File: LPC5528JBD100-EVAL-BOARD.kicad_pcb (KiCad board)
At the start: 2 copper layers, 100 x 100 mm, 45 parts, among them J1 Jack-DC, J2 USB_B_Micro, J3 MCU_VOLTAGE_SEL, U1 LM2596S-5, U2 LPC55S28JBD100, U3 LM1117-3.3, U4 LM1117-1.8, U5 TPS2552DBVR, Y1 24MHz

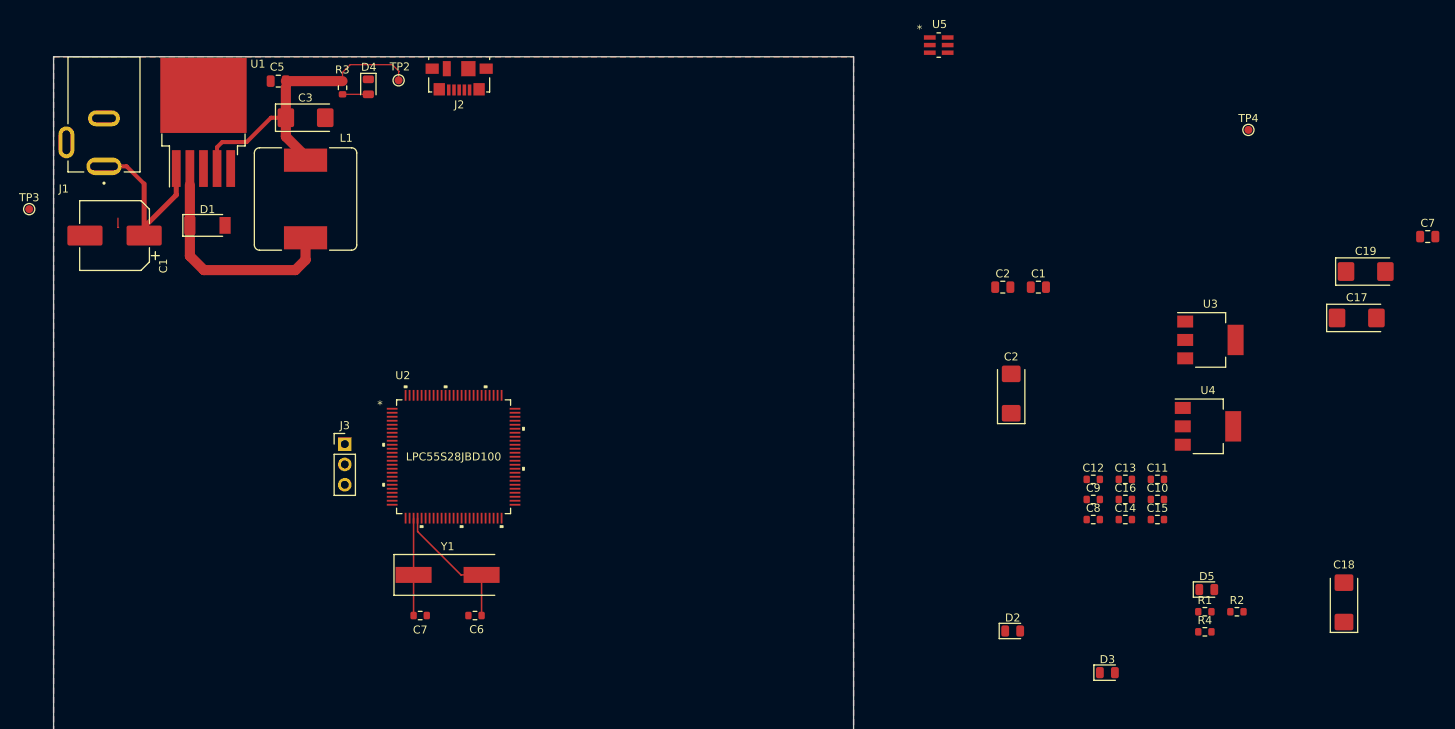
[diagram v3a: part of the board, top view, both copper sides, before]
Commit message: USB Current limiting devresi tamamlanacak. ADC bağlantıları yapılıyor
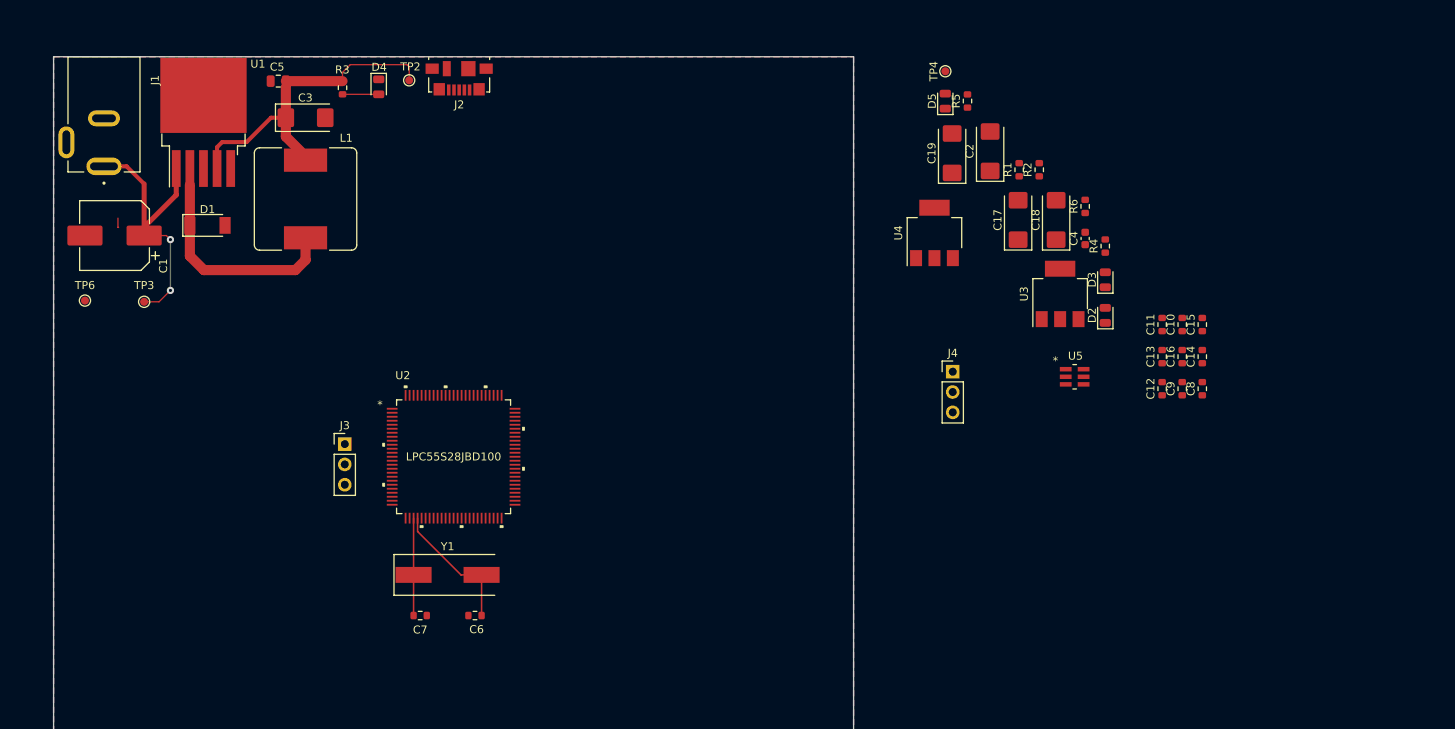
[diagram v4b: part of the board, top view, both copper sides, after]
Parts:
- removed the C1 at (123.1, 28.8)
- removed the C2 at (119.7, 42.1)
- removed the C2 at (118.7, 28.8)
- removed the C7 at (171.8, 22.5)
- added C2: 10uF, Capacitor_Tantalum_SMD:CP_EIA-6032-28_Kemet-C, F.Cu at (117.1, 11.8)
- added C4: 0.1uF, Capacitor_SMD:C_0603_1608Metric, F.Cu at (128.9, 22.7)
- added J4: ADC_V_SELECT, Connector_PinHeader_2.54mm:PinHeader_1x03_P2.54mm_Vertical, F.Cu at (112.4, 39.4)
- added R5: 20k, Resistor_SMD:R_0603_1608Metric, F.Cu at (114.2, 5.54)
- added R6: 100k, Resistor_SMD:R_0603_1608Metric, F.Cu at (128.9, 18.7)
- added TP6: TP_GND, TestPoint:TestPoint_Pad_D1.0mm, F.Cu at (3.92, 30.5)
- J3: value MCU_VOLTAGE_SEL -> MCU_V_SEL
- moved D5 69.3 mm to (111.5, 5.55), turned to 90 degrees
- moved R2 60.5 mm to (123.2, 14.1), turned to 90 degrees
- moved R1 59.9 mm to (120.7, 14.1), turned to 90 degrees
- moved C18 59.8 mm to (125.3, 20.4)
- moved C19 53.8 mm to (112.3, 12.1), turned to 90 degrees
- moved R4 49.8 mm to (131.5, 23.7), turned to 90 degrees
- moved D3 49.1 mm to (131.5, 27.9), turned to 90 degrees
- moved U5 44.8 mm to (127.6, 40.0)
- moved C17 44.1 mm to (120.6, 20.4), turned to 90 degrees
- moved U4 41.9 mm to (110.1, 22.0), turned to 90 degrees
- moved D2 41.1 mm to (131.5, 32.3), turned to 90 degrees
- moved TP4 38.6 mm to (111.5, 1.82), turned to 90 degrees
- moved C15 25.0 mm to (143.6, 33.5), turned to 90 degrees
- moved C14 22.5 mm to (143.6, 37.5), turned to 90 degrees
- moved C10 22.1 mm to (141.1, 33.5), turned to 90 degrees
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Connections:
- C10 pad 1: +3V3 -> V_TARGET
- C11 pad 1: +3V3 -> V_TARGET
- C12 pad 1: +3V3 -> V_TARGET
- C13 pad 1: +3V3 -> V_TARGET
- C14 pad 1: +3V3 -> V_TARGET
- C15 pad 1: +3V3 -> V_TARGET
- C16 pad 1: +3V3 -> V_TARGET
- C8 pad 1: +3V3 -> V_TARGET
- C9 pad 1: +3V3 -> V_TARGET
- U2 pad 17: unconnected-(U2-Pad17) -> /MCU/MCU_VREFP
- U2 pad 18: unconnected-(U2-Pad18) -> /MCU/MCU_VREFN
- U5 pad 4: unconnected-(U5-Pad4) -> /Power/USB_FAULT
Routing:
- net V_IN: track 22.4 -> 36.1 mm, vias 0 -> 2
- net +5V: track 37.8 -> 39.3 mm
- net Net-(D4-Pad2): track 3.23 -> 4.52 mm

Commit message: MCU bölümlere ayrýldý
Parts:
- added C21: 47pF, Resistor_SMD:R_0603_1608Metric, F.Cu at (175.6, 76.0)
- added C22: 0.1uF, Resistor_SMD:R_0603_1608Metric, F.Cu at (156.1, 94.8)
- added C6: 18pF, Resistor_SMD:R_0603_1608Metric, F.Cu at (195.1, 82.2)
- added C7: 18pF, Resistor_SMD:R_0603_1608Metric, F.Cu at (191.1, 82.2)
- added J3: ADC_EXT_SUPPLY, Connector_PinHeader_2.54mm:PinHeader_1x03_P2.54mm_Vertical, F.Cu at (171.3, 86.7)
- added R10: 0, Resistor_SMD:R_0603_1608Metric, F.Cu at (152.1, 94.8)
- added R7: 0, Resistor_SMD:R_0603_1608Metric, F.Cu at (179.6, 76.0)
- added R8: 0, Resistor_SMD:R_0603_1608Metric, F.Cu at (160.2, 94.8)
- added R9: 0, Resistor_SMD:R_0603_1608Metric, F.Cu at (164.2, 94.8)
- added Y1: 24MHz, Crystal:Crystal_SMD_HC49-SD, F.Cu at (196.4, 77.8)
- J4: value ADC_V_SELECT -> MCU_V_SEL
- moved J4 69.9 mm to (171.3, 77.0)
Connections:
- C10 pad 1: V_TARGET -> VDD
- C11 pad 1: V_TARGET -> VDD
- C12 pad 1: V_TARGET -> VDD
- C13 pad 1: V_TARGET -> VDD
- C14 pad 1: V_TARGET -> VDD
- C15 pad 1: V_TARGET -> VDD
- C16 pad 1: V_TARGET -> VDD
- C8 pad 1: V_TARGET -> VDD
- C9 pad 1: V_TARGET -> VDD
- J4 pad 2: V_ADC -> V_TARGET
- U2 pad 100: /MCU/MCU_VDD -> VDD
- U2 pad 15: /MCU/MCU_VDD -> VDD
- U2 pad 16: /MCU/MCU_VDDA -> VDDA
- U2 pad 17: /MCU/MCU_VREFP -> /MCU/VREFP_TARGET
- U2 pad 18: /MCU/MCU_VREFN -> /MCU/VREFN_TARGET
- U2 pad 19: unconnected-(U2-Pad19) -> GND
- U2 pad 25: unconnected-(U2-Pad25) -> VDD
- U2 pad 28: /MCU/MCU_XTAL32M_N -> unconnected-(U2-Pad28)
- U2 pad 29: /MCU/MCU_XTAL32M_P -> /MCU_1/MCU_XTAL32M_P
- U2 pad 44: unconnected-(U2-Pad44) -> VDD
- U2 pad 46: unconnected-(U2-Pad46) -> GND
- U2 pad 47: unconnected-(U2-Pad47) -> GND
- U2 pad 52: unconnected-(U2-Pad52) -> /MCU_1/MCU_XTAL32M_N
- U2 pad 63: unconnected-(U2-Pad63) -> VDD
- U2 pad 69: unconnected-(U2-Pad69) -> VDD
- U2 pad 75: unconnected-(U2-Pad75) -> VDD
- U2 pad 84: unconnected-(U2-Pad84) -> VDD
- U2 pad 95: unconnected-(U2-Pad95) -> VDD

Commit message: Reset devresi eklenecek.
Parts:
- added C21: 47pF, Resistor_SMD:R_0603_1608Metric, F.Cu at (159.1, 45.1)
- added C22: 0.1uF, Resistor_SMD:R_0603_1608Metric, F.Cu at (163.1, 42.6)
- added C24: 47pF, Resistor_SMD:R_0603_1608Metric, F.Cu at (126.3, 56.0)
- added C25: 22uF, Resistor_SMD:R_0603_1608Metric, F.Cu at (155.0, 45.1)
- added C26: 100nF, Resistor_SMD:R_0603_1608Metric, F.Cu at (163.1, 45.1)
- added C27: 47pF, Resistor_SMD:R_0603_1608Metric, F.Cu at (159.1, 42.6)
- added C28: 22pF, Resistor_SMD:R_0603_1608Metric, F.Cu at (155.0, 42.6)
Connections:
- U2 pad 16: VDDA -> V_TARGET
- U2 pad 33: unconnected-(U2-Pad33) -> GND
- U2 pad 37: unconnected-(U2-Pad37) -> GND
- U2 pad 39: unconnected-(U2-Pad39) -> Net-(C28-Pad1)
- U2 pad 45: unconnected-(U2-Pad45) -> Net-(C28-Pad1)
- U2 pad 48: unconnected-(U2-Pad48) -> Net-(L2-Pad1)
- U2 pad 49: unconnected-(U2-Pad49) -> V_TARGET
- U2 pad 50: unconnected-(U2-Pad50) -> V_TARGET
- U2 pad 51: unconnected-(U2-Pad51) -> V_TARGET
- U2 pad 99: unconnected-(U2-Pad99) -> GND

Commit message: ISP Boot eklenecek
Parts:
- removed the C21 at (159.1, 45.1)
- removed the C21 at (175.6, 76.0)
- removed the C22 at (163.1, 42.6)
- removed the C22 at (156.1, 94.8)
- removed C24: 47pF, Resistor_SMD:R_0603_1608Metric
- removed the C6 at (195.1, 82.2)
- removed the C7 at (191.1, 82.2)
- removed the J3 at (171.3, 86.7)
- removed U2: LPC55S28JBD100, erkan-hw-lib:HLQFP100
- removed the Y1 at (196.4, 77.8)
- added C20: 120uF, Capacitor_Tantalum_SMD:CP_EIA-6032-28_Kemet-C, F.Cu at (227.4, 19.3)
- added C21: 47pF, Capacitor_SMD:C_0603_1608Metric, F.Cu at (260.3, 18.5)
- added C22: 0.1uF, Capacitor_SMD:C_0603_1608Metric, F.Cu at (256.1, 23.5)
- added C23: 10nF, Capacitor_SMD:C_0603_1608Metric, F.Cu at (256.2, 13.4)
- added C29: 47pF, Capacitor_SMD:C_0603_1608Metric, F.Cu at (264.3, 13.4)
- added C30: 100nF, Capacitor_SMD:C_0603_1608Metric, F.Cu at (256.2, 16.0)
- added C31: 2.2uF, Capacitor_SMD:C_0603_1608Metric, F.Cu at (252.2, 16.0)
- added C32: 10uF, Capacitor_SMD:C_0603_1608Metric, F.Cu at (177.9, 13.4)
- added C33: 10uF, Capacitor_SMD:C_0603_1608Metric, F.Cu at (185.9, 13.4)
- added J5: JLink-1, Connector_PinHeader_1.27mm:PinHeader_2x05_P1.27mm_Vertical, F.Cu at (53.5, 34.3)
- added J6: JLink-2, Connector_IDC:IDC-Header_2x05_P2.54mm_Vertical, F.Cu at (195.2, 54.6)
- added J7: Conn_01x40, Connector_PinSocket_2.54mm:PinSocket_1x40_P2.54mm_Vertical, F.Cu at (69.3, 43.2)
- added J8: Conn_01x40, Connector_PinSocket_2.54mm:PinSocket_1x40_P2.54mm_Vertical, F.Cu at (22.2, 92.8)
- added L2: 4.7uH, Inductor_SMD:L_0805_2012Metric, F.Cu at (247.9, 23.3)
- added R11: 0, Resistor_SMD:R_0603_1608Metric, F.Cu at (189.9, 13.4)
- added R12: 0, Resistor_SMD:R_0603_1608Metric, F.Cu at (169.8, 13.4)
- added R13: 100k, Resistor_SMD:R_0603_1608Metric, F.Cu at (169.8, 16.0)
- added R14: 100k, Resistor_SMD:R_0603_1608Metric, F.Cu at (173.8, 13.4)
- added R15: 100k, Resistor_SMD:R_0603_1608Metric, F.Cu at (181.9, 13.4)
- added R16: 100k, Resistor_SMD:R_0603_1608Metric, F.Cu at (152.4, 35.9)
- added R17: 100, Resistor_SMD:R_0603_1608Metric, F.Cu at (164.3, 21.9)
- added SW1: SW_SPST, Button_Switch_SMD:SW_SPST_CK_RS282G05A3, F.Cu at (146.6, 118.4)
- C10, C11, C12, C13, C14, C15, C16, C25, C26, C27, C6, C7, C8, C9: footprint Resistor_SMD:R_0603_1608Metric -> Capacitor_SMD:C_0603_1608Metric
- C28: value 22pF -> 22uF; footprint Resistor_SMD:R_0603_1608Metric -> Capacitor_SMD:C_0603_1608Metric
- C5: footprint Capacitor_SMD:C_0805_2012Metric -> Capacitor_SMD:C_0603_1608Metric
- D1: footprint erkan-hw-lib:D_SOD-128 -> Diode_SMD:D_SOD-128
- J1: value Jack-DC -> Barrel_Jack_MountingPin
- J3: value MCU_V_SEL -> ADC_EXT_SUPPLY
- U5: value TPS2552DBVR -> DBV6
- Y1: value 24MHz -> 16MHz
- moved C16 129.4 mm to (268.3, 13.4), turned to 0 degrees
- moved R8 129.0 mm to (260.3, 13.4)
- moved C15 125.9 mm to (268.3, 16.0), turned to 0 degrees
- moved R9 124.3 mm to (260.3, 16.0)
- moved C10 123.7 mm to (264.2, 21.0), turned to 0 degrees
- moved TP4 123.3 mm to (233.2, 21.5), turned to 0 degrees
- moved C2 119.0 mm to (236.0, 14.6), turned to 0 degrees
- moved C8 118.4 mm to (260.2, 21.0), turned to 0 degrees
- moved R10 117.7 mm to (247.6, 25.9)
- moved C14 117.4 mm to (260.2, 23.5), turned to 0 degrees
- moved C11 117.3 mm to (255.6, 26.0), turned to 0 degrees
- moved C12 117.1 mm to (252.2, 13.4), turned to 0 degrees
- moved R5 116.4 mm to (228.8, 26.0), turned to 0 degrees
- moved C13 115.2 mm to (252.2, 18.5), turned to 0 degrees
- moved C19 115.1 mm to (227.4, 14.6), turned to 0 degrees
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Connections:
- C10 pad 1: VDD -> V_TARGET
- C11 pad 1: VDD -> V_TARGET
- C12 pad 1: VDD -> V_TARGET
- C13 pad 1: VDD -> V_TARGET
- C14 pad 1: VDD -> V_TARGET
- C15 pad 1: VDD -> V_TARGET
- C16 pad 1: VDD -> V_TARGET
- C4 pad 1: VBUS -> +5V
- C6 pad 1: /MCU/MCU_XTAL32M_P -> /MCU_1/MCU_XTAL32M_P
- C7 pad 1: /MCU/MCU_XTAL32M_N -> /MCU_1/MCU_XTAL32M_N
- C8 pad 1: VDD -> V_TARGET
- C9 pad 1: VDD -> V_TARGET
- J2 pad 1: VBUS -> +5V
- J3 pad 1: +3V3 -> /MCU/ADC_VREFN
- J3 pad 2: V_TARGET -> GND
- J3 pad 3: +1V8 -> /MCU/ADC_VREFP
- R7 pad 1: /MCU/VDDA_TARGET -> V_TARGET
- U5 pad 1: VBUS -> +5V
- U5 pad 6: +5V -> VBUS
- Y1 pad 1: /MCU/MCU_XTAL32M_N -> /MCU_1/MCU_XTAL32M_N
- Y1 pad 2: /MCU/MCU_XTAL32M_P -> /MCU_1/MCU_XTAL32M_P
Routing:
- net /MCU/MCU_XTAL32M_P: track 17.0 -> 0.00 mm
- net /MCU_1/MCU_XTAL32M_P: track 0.00 -> 12.5 mm
- net /MCU/MCU_XTAL32M_N: track 12.2 -> 0.00 mm
- net /MCU_1/MCU_XTAL32M_N: track 0.00 -> 10.4 mm
- net +5V: vias 0 -> 1

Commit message: Schematic updated
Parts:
- added J9: VBus-Select, Connector_PinHeader_2.54mm:PinHeader_1x03_P2.54mm_Vertical, F.Cu at (35.0, 1.82)
- added U2: LPC55S28JBD100, erkan-hw-lib:HLQFP100, F.Cu at (8.93, 8.91)
- J8: value Conn_01x40 -> Conn_02x20; footprint Connector_PinSocket_2.54mm:PinSocket_1x40_P2.54mm_Vertical -> Connector_PinSocket_2.54mm:PinSocket_2x20_P2.54mm_Vertical
- R5: value 20k -> 47k
- SW1: footprint Button_Switch_SMD:SW_SPST_CK_RS282G05A3 -> Button_Switch_SMD:SW_SPST_PTS645
- U5: value DBV6 -> TPS2552DBVR
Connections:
- R6 pad 1: VBUS -> +5V
